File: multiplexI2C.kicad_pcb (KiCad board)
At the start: 2 copper layers, 48.3 x 71.1 mm, 101 parts, among them J1 Screw_Terminal_01x04, J18 Conn_02x04_Top_Bottom, J2 Screw_Terminal_01x04, J20 Screw_Terminal_01x02, J3 Screw_Terminal_01x04, J4 Screw_Terminal_01x04, J5 Screw_Terminal_01x04, J6 Screw_Terminal_01x04, J7 Screw_Terminal_01x04, J8 Screw_Terminal_01x04, SW1 SW_Push, SW2 SW_Push, U1 PCA9548A, U2 RFM95W-915S2, U5 STM32F411CEU6, U6 AMS1117-3.3 SOT-223, Y1 25MHz, Y2 32.758kHz

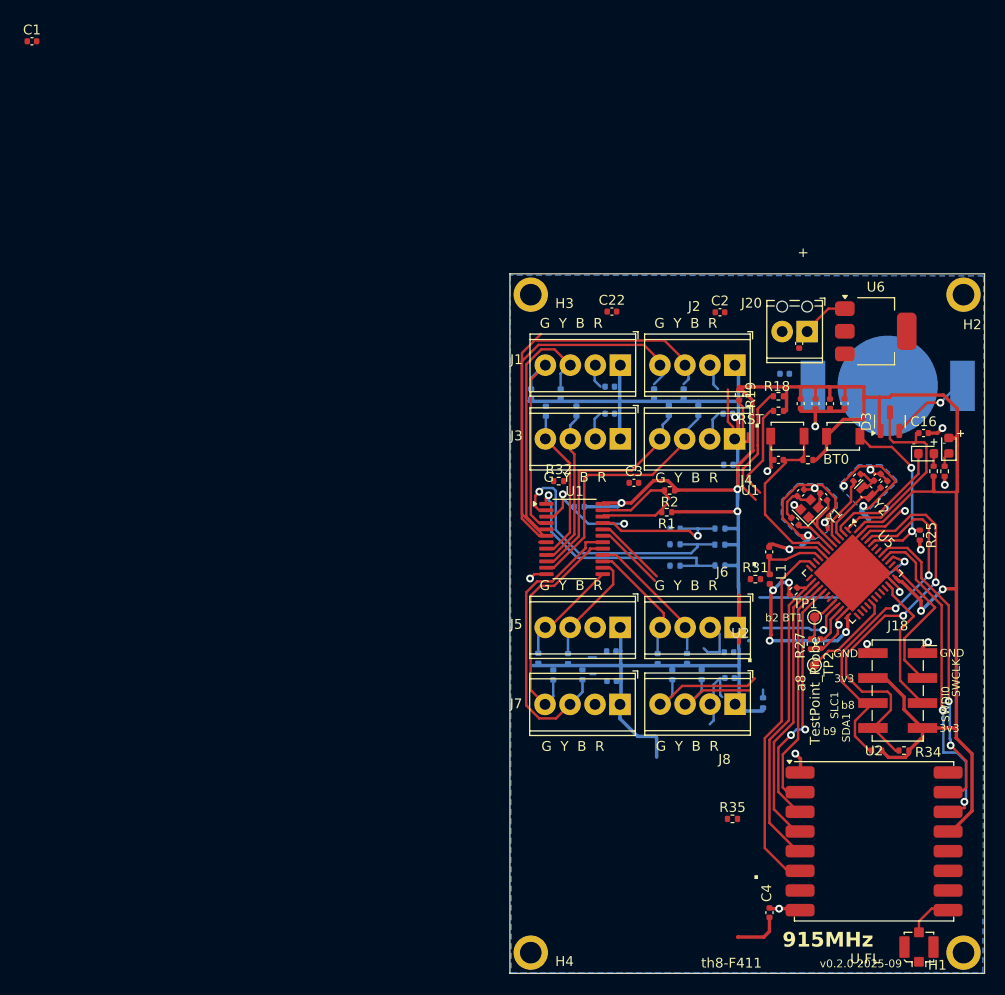
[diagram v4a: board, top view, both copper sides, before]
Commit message: adding MCU, ongoing.
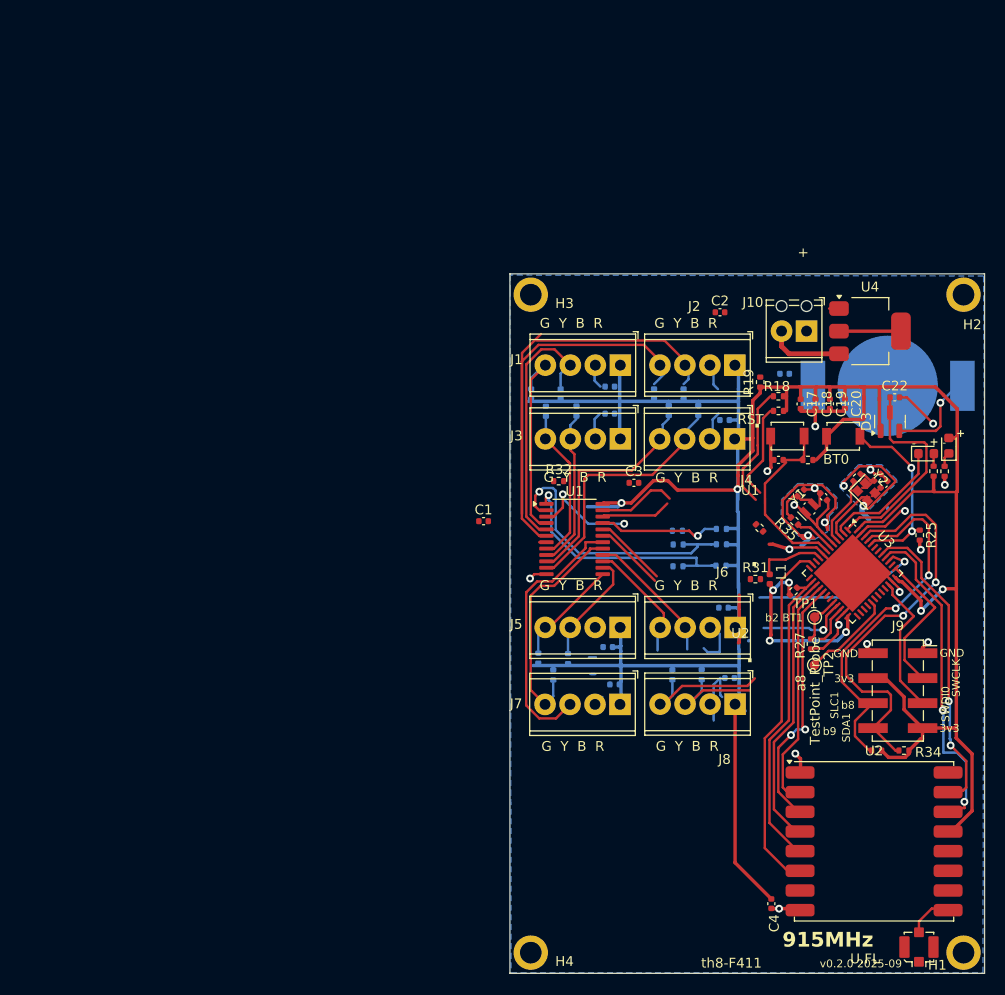
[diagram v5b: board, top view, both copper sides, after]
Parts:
- removed the C14 at (81.1, 61.7)
- removed the C15 at (78.9, 31.2)
- removed the C16 at (91.6, 40.3)
- removed the C17 at (75.9, 52.4)
- removed the C9 at (71.7, 43.5)
- removed J18: Conn_02x04_Top_Bottom, ProjectLib:PinSocket_2x04_P2.54mm_Vertical_SMD
- removed J20: Screw_Terminal_01x02, ProjectLib:TerminalBlock_Phoenix_MPT-0,5-2-2.54_1x02_P2.54mm_Horizontal
- removed the R17 at (67.5, 63.2)
- removed the R18 at (64.5, 63.3)
- removed the R19 at (56.9, 64.9)
- removed the R23 at (66.3, 51.6)
- removed the R24 at (70.9, 50.0)
- removed the R25 at (66.3, 50.0)
- removed the R26 at (75.3, 67.7)
- removed U5: STM32F411CEU6, Package_DFN_QFN:QFN-48-1EP_7x7mm_P0.5mm_EP5.6x5.6mm
- removed U6: AMS1117-3.3 SOT-223, Package_TO_SOT_SMD:SOT-223-3_TabPin2
- added J10: Screw_Terminal_01x02, ProjectLib:TerminalBlock_Phoenix_MPT-0,5-2-2.54_1x02_P2.54mm_Horizontal, F.Cu at (79.7, 29.9)
- added J9: Conn_02x04_Top_Bottom, ProjectLib:PinSocket_2x04_P2.54mm_Vertical_SMD, F.Cu at (89.0, 66.5)
- added U3: STM32F411CEU6, Package_DFN_QFN:QFN-48-1EP_7x7mm_P0.5mm_EP5.6x5.6mm, F.Cu at (84.4, 54.6)
- added U4: AMS1117-3.3 SOT-223, Package_TO_SOT_SMD:SOT-223-3_TabPin2, F.Cu at (86.1, 30.0)
- C10: value 10pF C0G, NP0, +/- 0.1pF -> 100nF
- C11: value 10pF C0G, NP0, +/- 0.1pF -> 4.7µF
- C12: value 4pF C0G, NP0, +/- 0.1pF -> 100nF
- C14: value 4.7µF -> 4pF C0G, NP0, +/- 0.1pF
- C15, C16: value 100nF -> 10pF C0G, NP0, +/- 0.1pF
- C17: value 100nF -> 1µF; moved to F.Cu
- C18, C19, C20: value 0.1µF -> 100nF; moved to F.Cu
- C21, C22: value 0.1µF -> 100nF
- C5: value 1µF -> 0.1µF; moved to B.Cu
- C6, C7, C8: value 100nF -> 0.1µF; moved to B.Cu
- C9: value 100nF -> 0.1µF
- R1, R2: moved to B.Cu
- R23: value 715 1% -> 4.7k
- R24: value 280 1% -> 4.7k
- R25: value 10k 1% -> 4.7k
- R27: value 10k 1% -> 715 1%
- R28: value 10k 1% -> 280 1%
- R29: value 0 -> 10k 1%
- R30: value 634 1% -> 10k 1%
- R32: value 10k -> 10k 1%
- R34: value 10k 1% -> 0
- R35: value 10k 1% -> 634 1%
- R7, R8: value 4.7k -> 10k 1%
- R9: value 4.7k -> 10k
- Y1: value 25MHz -> 32.758kHz; footprint ProjectLib:Crystal_SMD_2016-4Pin_2.0x1.6mm -> ProjectLib:Crystal_SMD_MicroCrystal_CM9V-T1A-2Pin_1.6x1.0mm
- Y2: value 32.758kHz -> 25MHz; footprint ProjectLib:Crystal_SMD_MicroCrystal_CM9V-T1A-2Pin_1.6x1.0mm -> ProjectLib:Crystal_SMD_2016-4Pin_2.0x1.6mm
- moved C1 67.0 mm to (46.9, 49.3)
- moved C20 36.8 mm to (83.6, 37.3), turned to -90 degrees
- moved C8 34.3 mm to (60.2, 65.9), turned to 180 degrees
- moved C6 33.5 mm to (59.5, 62.1), turned to 180 degrees
- moved C18 32.6 mm to (80.6, 37.4), turned to -90 degrees
- moved R35 30.9 mm to (78.5, 49.3), turned to 135 degrees
- moved C22 30.1 mm to (88.7, 36.7)
- moved C19 27.2 mm to (82.1, 37.4), turned to -90 degrees
- moved C7 22.8 mm to (71.2, 58.1), turned to 180 degrees
- moved C5 12.3 mm to (71.4, 39.0), turned to 180 degrees
- moved R3 10.3 mm to (66.6, 50.3)
- moved C17 7.47 mm to (79.1, 37.4), turned to -90 degrees
- moved R1 5.62 mm to (66.6, 53.9)
- moved R2 5.56 mm to (66.6, 51.6)
- moved R4 4.67 mm to (71.0, 53.8)
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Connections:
- C10 pad 1: GND_HSE -> GND
- C10 pad 2: Net-(C10-Pad2) -> Net-(U3-NRST)
- C11 pad 1: GND_HSE -> Net-(U3-VCAP1)
- C11 pad 2: PH0_OSC_IN -> GND
- C12 pad 1: GND_LSE -> Net-(U3-VDDA/VREF+)
- C12 pad 2: PC14_OSC32_IN -> GND
- C13 pad 2: Net-(C13-Pad2) -> PC14_OSC32_IN
- C14 pad 1: Net-(U5-VCAP1) -> GND_LSE
- C14 pad 2: GND -> Net-(C14-Pad2)
- C15 pad 1: +5V -> GND_HSE
- C15 pad 2: GND -> PH0_OSC_IN
- C16 pad 1: VBAT -> GND_HSE
- C16 pad 2: GND -> Net-(C16-Pad2)
- C17 pad 1: Net-(U5-VDDA/VREF+) -> +3V3
- C21 pad 1: +3V3 -> +5V
- C22 pad 1: +3V3 -> VBAT
- C9 pad 1: GND -> +3V3
- C9 pad 2: Net-(U5-NRST) -> GND
- L1 pad 1: Net-(U5-VDDA/VREF+) -> Net-(U3-VDDA/VREF+)
- NT1 pad 2: GND_HSE -> GND_LSE
- NT2 pad 2: GND_LSE -> GND_HSE
- R10 pad 2: /Connector1/SD -> /Connector0/SC
- R11 pad 2: /Connector2/SC -> /Connector0/SD
- R12 pad 2: /Connector2/SD -> /Connector1/SC
- R13 pad 2: /Connector3/SC -> /Connector1/SD
- R14 pad 2: /Connector3/SD -> /Connector2/SC
- R15 pad 2: /Connector4/SC -> /Connector2/SD
- R16 pad 2: /Connector4/SD -> /Connector3/SC
- R17 pad 2: /Connector5/SC -> /Connector3/SD
- R18 pad 2: /Connector5/SD -> /Connector4/SC
- R19 pad 2: /Connector6/SC -> /Connector4/SD
- R20 pad 2: /Connector6/SD -> /Connector5/SC
- R21 pad 2: /Connector7/SC -> /Connector5/SD
- R22 pad 2: /Connector7/SD -> /Connector6/SC
- R23 pad 1: Net-(D1-K) -> +3V3
- R23 pad 2: GND -> /Connector6/SD
- R24 pad 2: Net-(D2-A) -> /Connector7/SC
- R25 pad 1: Net-(U5-BOOT0) -> +3V3
- R25 pad 2: GND -> /Connector7/SD
- R26 pad 2: Net-(U5-NRST) -> NSS
- R27 pad 1: Net-(U5-PB2) -> Net-(D1-K)
- R28 pad 2: SCL2 -> Net-(D2-A)
- R29 pad 1: PC15_OSC32_OUT -> Net-(U3-BOOT0)
- R29 pad 2: Net-(C13-Pad2) -> GND
- R30 pad 1: PH1_OSC_OUT -> +3V3
- R30 pad 2: Net-(C10-Pad2) -> Net-(U3-NRST)
- R31 pad 1: +3V3 -> Net-(U3-PB2)
- R31 pad 2: SDA2 -> GND
- R32 pad 1: +3V3 -> SDA1
- R32 pad 2: PA9 -> +3V3
- R34 pad 1: SDA1 -> PC15_OSC32_OUT
- R34 pad 2: +3V3 -> Net-(C14-Pad2)
- R35 pad 1: +3V3 -> PH1_OSC_OUT
- R35 pad 2: NSS -> Net-(C16-Pad2)
- R7 pad 2: /Connector0/SC -> SCL2
- R8 pad 2: /Connector0/SD -> SDA2
- R9 pad 2: /Connector1/SC -> PA9
- SW1 pad 1: GND -> +3V3
- SW1 pad 2: Net-(U5-NRST) -> Net-(U3-BOOT0)
- SW2 pad 1: +3V3 -> GND
- SW2 pad 2: Net-(U5-BOOT0) -> Net-(U3-NRST)
- TP1 pad 1: Net-(U5-PB2) -> Net-(U3-PB2)
- Y1 pad 1: PH0_OSC_IN -> Net-(C14-Pad2)
- Y1 pad 2: GND_HSE -> PC14_OSC32_IN
- Y2 pad 1: Net-(C13-Pad2) -> PH0_OSC_IN
- Y2 pad 2: PC14_OSC32_IN -> GND_HSE
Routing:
- net SDA1: track 41.9 -> 0.00 mm, vias 2 -> 0
- net PC15_OSC32_OUT: track 7.15 -> 49.0 mm, vias 0 -> 2
- net Net-(U5-BOOT0): track 19.1 -> 0.00 mm, vias 2 -> 0
- net Net-(U5-NRST): track 18.5 -> 0.00 mm
- net +3V3: track 300.3 -> 317.1 mm
- net /Connector5/SD: track 23.8 -> 11.6 mm
- net /Connector4/SC: track 10.9 -> 23.1 mm
- net PA9: track 0.00 -> 11.4 mm, vias 0 -> 2
- net GND: track 82.6 -> 71.5 mm, vias 15 -> 11
- net (no net): track 31.2 -> 42.0 mm, vias 2 -> 0
- net /Connector5/SC: track 23.6 -> 13.8 mm
- net /Connector3/SD: track 23.2 -> 33.0 mm
- net SDA2: track 18.0 -> 25.9 mm
- net +5V: track 0.00 -> 7.71 mm
- net SCL2: track 9.43 -> 16.5 mm
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
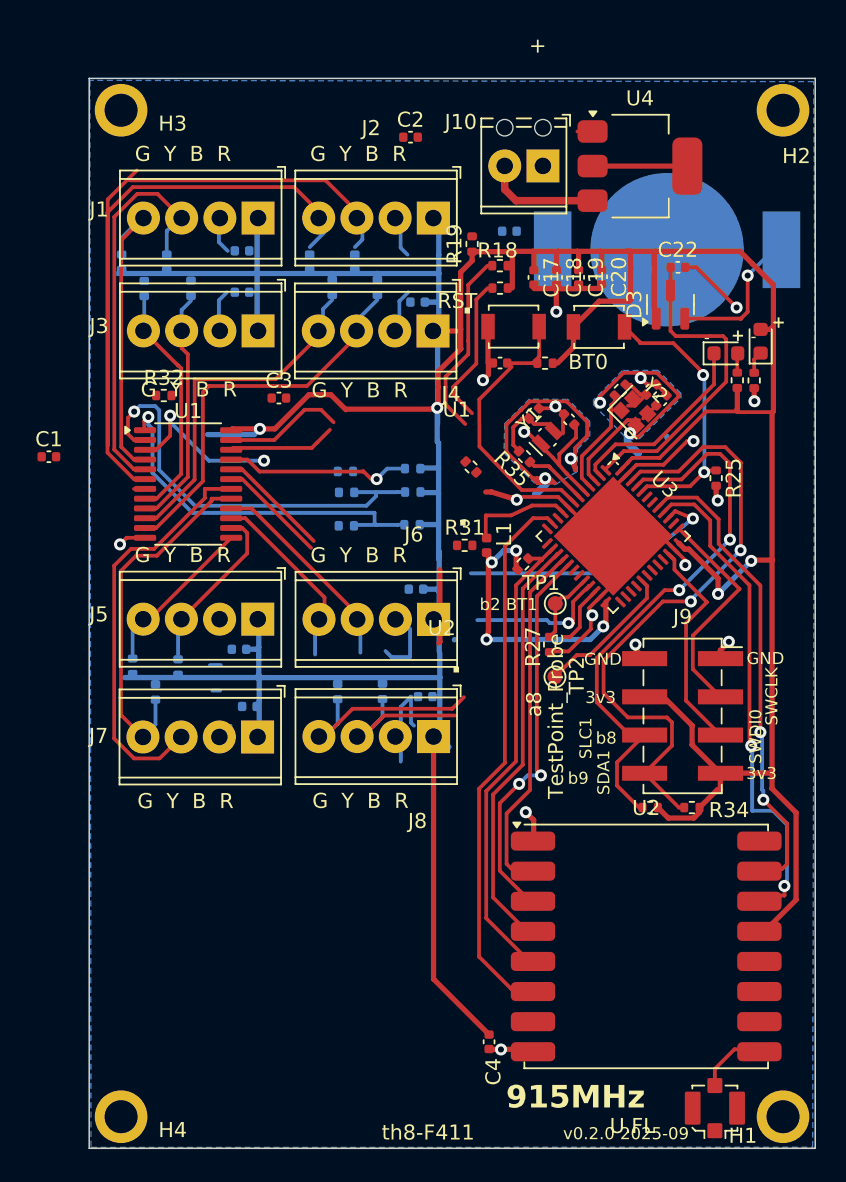
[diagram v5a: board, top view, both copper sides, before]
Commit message: th8-f411 with castellated MCU-LoRa. DRC clean, ERC with some warnings.
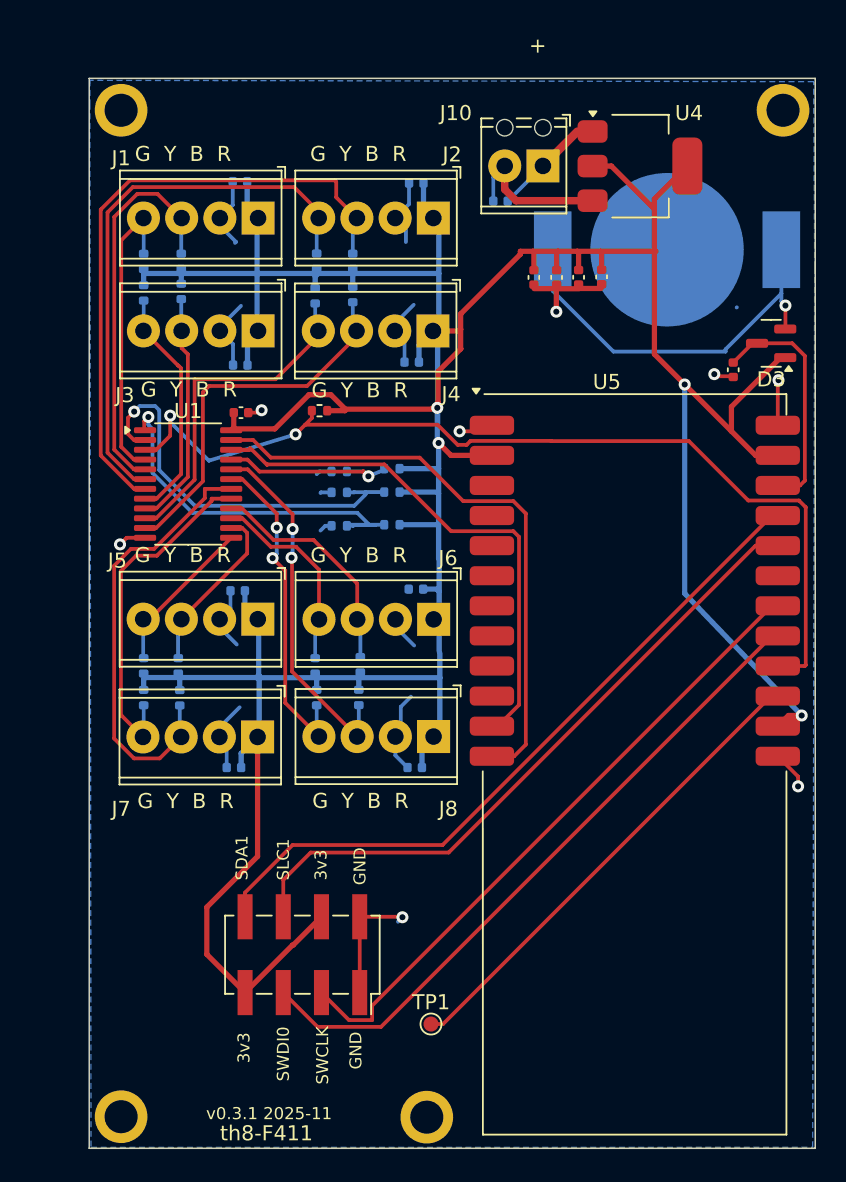
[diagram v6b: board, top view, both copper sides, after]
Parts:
- removed AE1: U.FL, ProjectLib:U.FL_Molex_MCRF_73412-0110_Vertical
- removed C10, C12: 100nF, ProjectLib:C_0402_1005Metric
- removed C11: 4.7µF, ProjectLib:C_0402_1005Metric
- removed C13, C14: 4pF C0G, NP0, +/- 0.1pF, ProjectLib:C_0402_1005Metric
- removed C15, C16: 10pF C0G, NP0, +/- 0.1pF, ProjectLib:C_0402_1005Metric
- removed D1: red 2ma 1.8Vf, ProjectLib:LED_0603_1608Metric
- removed D2: blue 2ma 2.65Vf, ProjectLib:LED_0603_1608Metric
- removed L1: 2.2uH, ProjectLib:L_0402_1005Metric
- removed NT1, NT2: NetTie_2, ProjectLib:NetTie-2_SMD_Pad0.5mm
- removed R26, R29, R30, R31, R32, R33, R7, R8: 10k 1%, ProjectLib:R_0402_1005Metric
- removed R27: 715 1%, ProjectLib:R_0402_1005Metric
- removed R28: 280 1%, ProjectLib:R_0402_1005Metric
- removed R34: 0, ProjectLib:R_0402_1005Metric
- removed R35: 634 1%, ProjectLib:R_0402_1005Metric
- removed SW1, SW2: SW_Push, ProjectLib:SW_SPST_B3U-1000P
- removed TP2: TestPoint_Probe, ProjectLib:TestPoint_Pad_D1.0mm
- removed U2: RFM95W-915S2, ProjectLib:HOPERF_RFM9XW_SMD
- removed U3: STM32F411CEU6, Package_DFN_QFN:QFN-48-1EP_7x7mm_P0.5mm_EP5.6x5.6mm
- removed Y1: 32.758kHz, ProjectLib:Crystal_SMD_MicroCrystal_CM9V-T1A-2Pin_1.6x1.0mm
- removed Y2: 25MHz, ProjectLib:Crystal_SMD_2016-4Pin_2.0x1.6mm
- added U5: f411-RFM95W, ProjectLib:Castellated_MCU-LoRa_20x50mm_2x12_P2.0mm_SMD, F.Cu at (85.8, 71.2)
- C2, C3, C4, C9, R17, R18, R19, R23, R24, R25: moved to B.Cu
- D3: footprint Package_TO_SOT_SMD:SOT-23 -> ProjectLib:SOT-23
- R9: moved to F.Cu
- TP1: value BT1 b2 -> TestPoint
- U1: footprint Package_SO:TSSOP-24_4.4x7.8mm_P0.65mm -> ProjectLib:TSSOP-24_4.4x7.8mm_P0.65mm
- U4: footprint Package_TO_SOT_SMD:SOT-223-3_TabPin2 -> ProjectLib:SOT-223
- moved C4 47.9 mm to (59.6, 43.2), turned to 180 degrees
- moved R23 45.7 mm to (53.1, 65.3)
- moved R19 35.5 mm to (53.1, 63.2)
- moved R18 34.1 mm to (55.5, 63.2), turned to 90 degrees
- moved C21 33.3 mm to (76.9, 32.3), turned to 0 degrees
- moved R24 32.8 mm to (67.5, 65.3), turned to -90 degrees
- moved R25 30.3 mm to (64.7, 65.3)
- moved J9 29.8 mm to (63.7, 82.4), turned to -90 degrees
- moved TP1 29.1 mm to (72.2, 87.0)
- moved R16 28.7 mm to (67.0, 38.5), turned to -90 degrees
- moved C9 27.5 mm to (71.2, 69.9), turned to 180 degrees
- moved R15 25.0 mm to (53.1, 38.4), turned to -90 degrees
- moved H1 23.7 mm to (72.0, 93.2)
- moved C3 17.0 mm to (71.3, 31.1), turned to 180 degrees
- moved R12 14.0 mm to (67.0, 36.3), turned to 90 degrees
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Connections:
- J9 pad b2: /f411/SWCLK -> /MCU-LoRa/SWCLK
- J9 pad b3: /f411/SWDIO -> /MCU-LoRa/SWDIO
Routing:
- net +3V3: track 317.1 -> 257.8 mm, vias 9 -> 4
- net PA9: track 11.4 -> 63.6 mm
- net PC15_OSC32_OUT: track 49.0 -> 0.00 mm, vias 2 -> 0
- net SDA1: track 0.00 -> 47.0 mm
- net /MCU-LoRa/SWDIO: track 0.00 -> 44.2 mm
- net /MCU-LoRa/SWCLK: track 0.00 -> 42.7 mm
- net (no net): track 42.0 -> 0.00 mm
- net RESET: track 36.6 -> 0.00 mm
- net DIO0: track 33.1 -> 0.00 mm, vias 2 -> 0
- net DIO1: track 31.6 -> 0.00 mm, vias 2 -> 0
- net Net-(U5-PA8-MCO): track 0.00 -> 31.6 mm
- net NSS: track 31.1 -> 0.00 mm
- net SCK: track 27.6 -> 0.00 mm
- net MOSI: track 25.6 -> 0.00 mm, vias 2 -> 0
- net MISO: track 23.8 -> 0.00 mm
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- removed copper zone on B.Cu, net GND_HSE
- removed copper zone on B.Cu, net GND_LSE
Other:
- board text added: "v0.3.1 2025-11"
- board text removed: "-"
- board text removed: "."
- board text removed: "915MHz"
- board text removed: "A0"
- board text removed: "A1"
- board text removed: "A2"
- board text removed: "BT0"
- board text removed: "RST"
- board text removed: "a8"
- board text removed: "b2 BT1"
- board text removed: "b8"
- board text removed: "b9"
- board text removed: "v0.2.0 2025-09"
